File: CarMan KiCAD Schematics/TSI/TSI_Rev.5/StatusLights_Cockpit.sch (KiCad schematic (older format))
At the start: 21 parts, among them U1 RDE03110S12

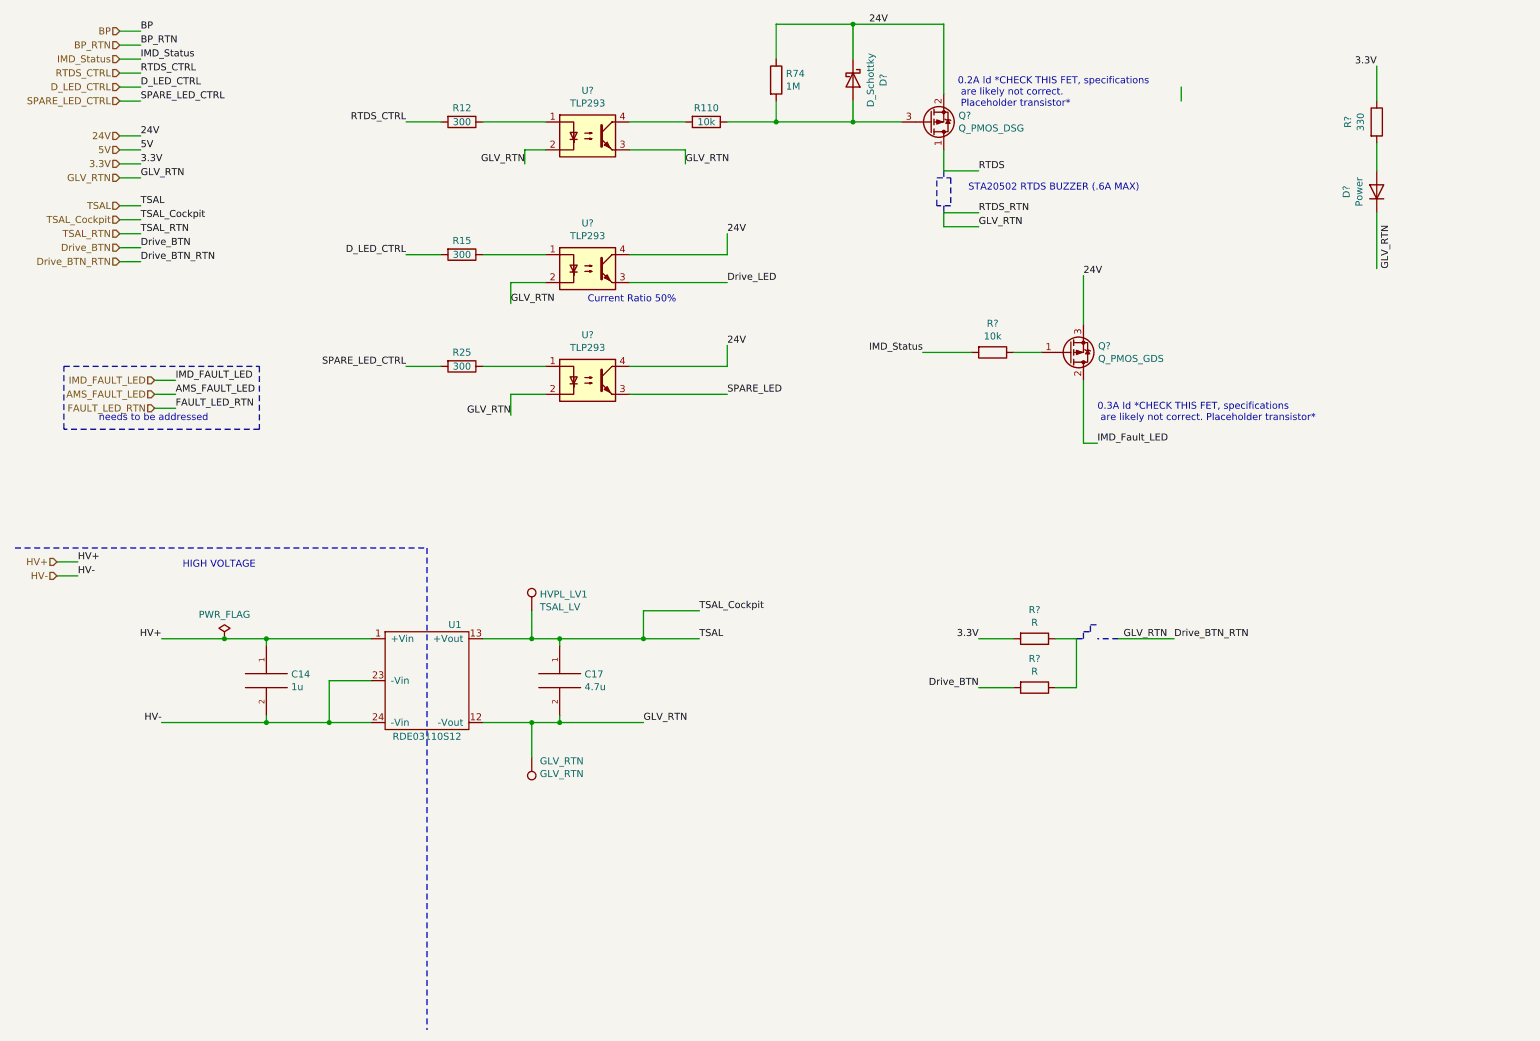
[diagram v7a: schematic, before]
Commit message: Res/Cap Value Updates & Organizational
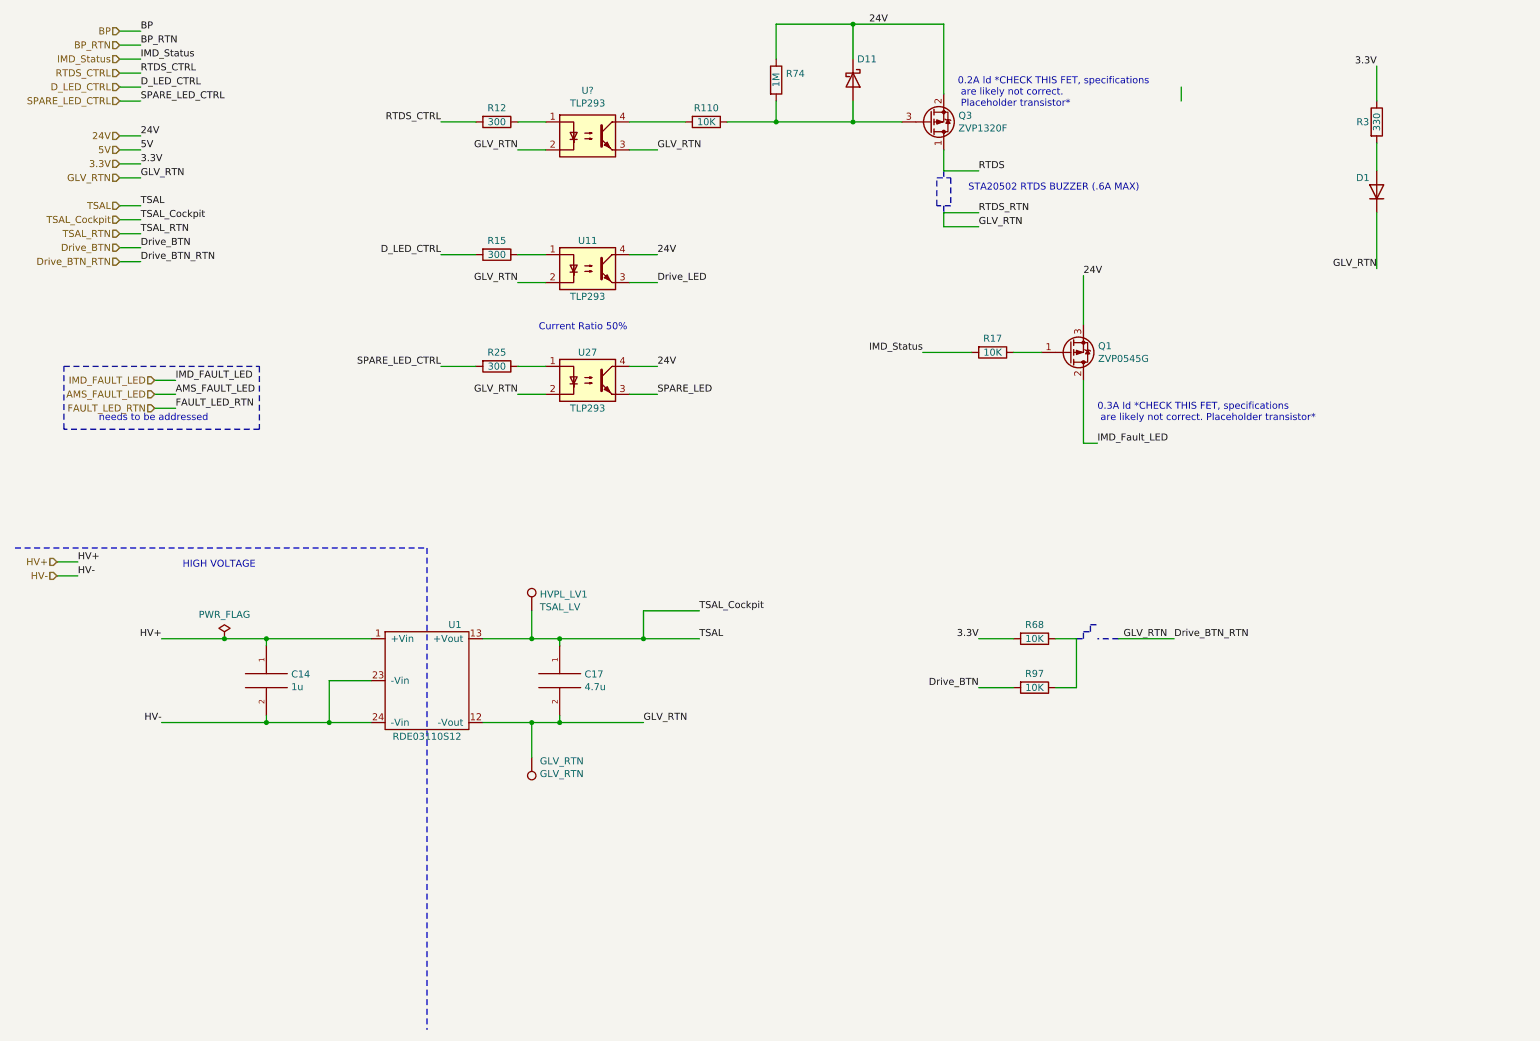
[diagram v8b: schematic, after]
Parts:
- Q1: renamed from Q?; value Q_PMOS_GDS -> ZVP0545G
- Q3: renamed from Q?; value Q_PMOS_DSG -> ZVP1320F
- R110: value 10k -> 10K
- R17: renamed from R?; value 10k -> 10K
- R68, R97: renamed from R?; value R -> 10K
- gave numbers to parts that had none: 5
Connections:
- wire segments 94 -> 88
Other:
- moved on the sheet: R12, R15, R25
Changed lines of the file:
@@
 EESchema Schematic File Version 4
-LIBS:TSI_Rev.5-cache
-EELAYER 29 0
+EELAYER 30 0
 EELAYER END
 $Descr A4 11693 8268
@@
 $EndDescr
 $Comp
-L Device:R R?
+L Device:R R3
 U 1 1 5F9997DD
 P 10200 1300
-F 0 "R?" V 9993 1300 50  0000 C CNN
-F 1 "330" V 10084 1300 50  0000 C CNN
+F 0 "R3" H 10100 1300 50  0000 C CNN
+F 1 "330" V 10200 1300 50  0000 C CNN
 F 2 "" V 10130 1300 50  0001 C CNN
 F 3 "~" H 10200 1300 50  0001 C CNN
@@
 $EndComp
 $Comp
-L Device:D D?
+L Device:D D1
 U 1 1 5F99A6B1
 P 10200 1800
-F 0 "D?" H 10200 2017 50  0000 C CNN
-F 1 "Power" H 10200 1926 50  0000 C CNN
+F 0 "D1" V 10300 1900 50  0000 C CNN
+F 1 "Power" H 10200 1926 50  0001 C CNN
 F 2 "" H 10200 1800 50  0001 C CNN
 F 3 "~" H 10200 1800 50  0001 C CNN
@@
 3.3V
 $Comp
-L TSI_Rev.5-rescue:TLP293-CarMan_KiCAD_Library-TSI_Rev.5-rescue U?
+L TSI_Rev.5-rescue:TLP293-CarMan_KiCAD_Library-TSI_Rev.5-rescue U11
 U 1 1 5F9A966C
 P 4550 2350
-F 0 "U?" H 4550 2675 50  0000 C CNN
-F 1 "TLP293" H 4550 2584 50  0000 C CNN
+F 0 "U11" H 4550 2550 50  0000 C CNN
+F 1 "TLP293" H 4550 2150 50  0000 C CNN
 F 2 "Package_SO:SOIC-4_4.55x2.6mm_P1.27mm" H 4350 2150 50  0001 L CIN
 F 3 "" H 4550 2350 50  0001 L CNN
@@
 $EndComp
 $Comp
-L TSI_Rev.5-rescue:TLP293-CarMan_KiCAD_Library-TSI_Rev.5-rescue U?
+L TSI_Rev.5-rescue:TLP293-CarMan_KiCAD_Library-TSI_Rev.5-rescue U27
 U 1 1 5F9AA400
 P 4550 3150
-F 0 "U?" H 4550 3475 50  0000 C CNN
-F 1 "TLP293" H 4550 3384 50  0000 C CNN
+F 0 "U27" H 4550 3350 50  0000 C CNN
+F 1 "TLP293" H 4550 2950 50  0000 C CNN
 F 2 "Package_SO:SOIC-4_4.55x2.6mm_P1.27mm" H 4350 2950 50  0001 L CIN
 F 3 "" H 4550 3150 50  0001 L CNN
@@
 	1    0    0    -1
 $EndComp
-Wire Wire Line
-	4850 2250 5550 2250
-Wire Wire Line
-	5550 2250 5550 2100
-Wire Wire Line
-	4850 2450 5550 2450
-Wire Wire Line
-	4850 3050 5550 3050
-Wire Wire Line
-	5550 3050 5550 2900
-Wire Wire Line
-	4850 3250 5550 3250
-Wire Wire Line
-	4250 2450 4000 2450
-Wire Wire Line
-	4000 2450 4000 2600
-Wire Wire Line
-	4250 3250 4000 3250
-Wire Wire Line
-	4000 3250 4000 3400
-$Comp
-L CarMan_KiCAD_Library:D_Schottky D?
+$Comp
+L CarMan_KiCAD_Library:D_Schottky D11
 U 1 1 5F9B6857
 P 6450 1000
-F 0 "D?" H 6450 1217 50  0000 C CNN
-F 1 "D_Schottky" H 6450 1126 50  0000 C CNN
+F 0 "D11" V 6300 1100 50  0000 C CNN
+F 1 "D_Schottky" H 6450 1126 50  0001 C CNN
 F 2 "" H 6450 1000 50  0001 C CNN
 F 3 "~" H 6450 1000 50  0001 C CNN
@@
 	0    1    1    0
 $EndComp
-Wire Wire Line
-	4100 1500 4100 1600
 $Comp
 L Device:R R12
 U 1 1 5F9BA8EE
-P 3650 1300
-F 0 "R12" V 3550 1300 50  0000 C CNN
-F 1 "300" V 3650 1300 50  0000 C CNN
-F 2 "" V 3580 1300 50  0001 C CNN
-F 3 "~" H 3650 1300 50  0001 C CNN
-	1    3650 1300
-	0    1    1    0
-$EndComp
-Wire Wire Line
-	3500 1300 3250 1300
-Text Label 3250 1300 2    50   ~ 0
+P 3900 1300
+F 0 "R12" V 3800 1300 50  0000 C CNN
+F 1 "300" V 3900 1300 50  0000 C CNN
+F 2 "" V 3830 1300 50  0001 C CNN
+F 3 "~" H 3900 1300 50  0001 C CNN
+	1    3900 1300
+	0    1    1    0
+$EndComp
+Wire Wire Line
+	3750 1300 3500 1300
+Text Label 3500 1300 2    50   ~ 0
 RTDS_CTRL
-Text Label 4100 1600 2    50   ~ 0
+Text Label 4050 1500 2    50   ~ 0
 GLV_RTN
 $Comp
@@
 P 5400 1300
 F 0 "R110" V 5300 1300 50  0000 C CNN
-F 1 "10k" V 5400 1300 50  0000 C CNN
+F 1 "10K" V 5400 1300 50  0000 C CNN
 F 2 "" V 5330 1300 50  0001 C CNN
 F 3 "~" H 5400 1300 50  0001 C CNN
@@
 P 5900 1000
 F 0 "R74" H 5970 1046 50  0000 L CNN
-F 1 "1M" H 5970 955 50  0000 L CNN
+F 1 "1M" V 5900 950 50  0000 L CNN
 F 2 "" V 5830 1000 50  0001 C CNN
 F 3 "~" H 5900 1000 50  0001 C CNN
@@
 L Device:R R15
 U 1 1 5F9DEF51
-P 3650 2250
-F 0 "R15" V 3550 2250 50  0000 C CNN
-F 1 "300" V 3650 2250 50  0000 C CNN
-F 2 "" V 3580 2250 50  0001 C CNN
-F 3 "~" H 3650 2250 50  0001 C CNN
-	1    3650 2250
-	0    1    1    0
-$EndComp
-Wire Wire Line
-	3800 2250 4250 2250
-Wire Wire Line
-	3500 2250 3250 2250
-Text Label 5550 2100 0    50   ~ 0
+P 3900 2250
+F 0 "R15" V 3800 2250 50  0000 C CNN
+F 1 "300" V 3900 2250 50  0000 C CNN
+F 2 "" V 3830 2250 50  0001 C CNN
+F 3 "~" H 3900 2250 50  0001 C CNN
+	1    3900 2250
+	0    1    1    0
+$EndComp
+Wire Wire Line
+	3750 2250 3500 2250
+Text Label 5050 2250 0    50   ~ 0
 24V
-Text Label 5550 2450 0    50   ~ 0
+Text Label 5050 2450 0    50   ~ 0
 Drive_LED
-Text Label 4000 2600 0    50   ~ 0
-GLV_RTN
-Text Label 3250 2250 2    50   ~ 0
+Text Label 4050 2450 2    50   ~ 0
+GLV_RTN
+Text Label 3500 2250 2    50   ~ 0
 D_LED_CTRL
 Wire Wire Line
@@
 Wire Wire Line
 	6450 600  7100 600
-Wire Wire Line
-	5250 1500 5250 1600
-Wire Wire Line
-	4250 1500 4100 1500
-Wire Wire Line
-	4250 1300 3800 1300
 $Comp
 L TSI_Rev.5-rescue:TLP293-CarMan_KiCAD_Library-TSI_Rev.5-rescue U?
@@
 	1    0    0    -1
 $EndComp
-Wire Wire Line
-	4850 1500 5250 1500
-Text Label 5250 1600 0    50   ~ 0
+Text Label 5050 1500 0    50   ~ 0
 GLV_RTN
 $Comp
 L Device:R R25
 U 1 1 5F9F8E38
-P 3650 3050
-F 0 "R25" V 3550 3050 50  0000 C CNN
-F 1 "300" V 3650 3050 50  0000 C CNN
-F 2 "" V 3580 3050 50  0001 C CNN
-F 3 "~" H 3650 3050 50  0001 C CNN
-	1    3650 3050
-	0    1    1    0
-$EndComp
-Wire Wire Line
-	3800 3050 4250 3050
-Wire Wire Line
-	3500 3050 3250 3050
-Text Label 4000 3400 2    50   ~ 0
-GLV_RTN
-Text Label 5550 3250 0    50   ~ 0
+P 3900 3050
+F 0 "R25" V 3800 3050 50  0000 C CNN
+F 1 "300" V 3900 3050 50  0000 C CNN
+F 2 "" V 3830 3050 50  0001 C CNN
+F 3 "~" H 3900 3050 50  0001 C CNN
+	1    3900 3050
+	0    1    1    0
+$EndComp
+Wire Wire Line
+	3750 3050 3500 3050
+Text Label 4050 3250 2    50   ~ 0
+GLV_RTN
+Text Label 5050 3250 0    50   ~ 0
 SPARE_LED
-Text Label 5550 2900 0    50   ~ 0
+Text Label 5050 3050 0    50   ~ 0
 24V
-Text Label 3250 3050 2    50   ~ 0
+Text Label 3500 3050 2    50   ~ 0
 SPARE_LED_CTRL
 $Comp
-L Device:Q_PMOS_DSG Q?
+L Device:Q_PMOS_DSG Q3
 U 1 1 5FA04A44
 P 7000 1300
-F 0 "Q?" H 7205 1254 50  0000 L CNN
-F 1 "Q_PMOS_DSG" H 7205 1345 50  0000 L CNN
+F 0 "Q3" H 7205 1254 50  0000 L CNN
+F 1 "ZVP1320F" H 7205 1345 50  0000 L CNN
 F 2 "" H 7200 1400 50  0001 C CNN
 F 3 "~" H 7000 1300 50  0001 C CNN
@@
 TSAL_Cockpit
 $Comp
-L Device:R R?
+L Device:R R17
 U 1 1 5FA5E58C
 P 7450 2950
-F 0 "R?" V 7243 2950 50  0000 C CNN
-F 1 "10k" V 7334 2950 50  0000 C CNN
+F 0 "R17" V 7350 2950 50  0000 C CNN
+F 1 "10K" V 7450 2950 50  0000 C CNN
 F 2 "" V 7380 2950 50  0001 C CNN
 F 3 "~" H 7450 2950 50  0001 C CNN
@@
 IMD_Status
 $Comp
-L Device:Q_PMOS_GDS Q?
+L Device:Q_PMOS_GDS Q1
 U 1 1 5FA66ED5
 P 8000 2950
-F 0 "Q?" H 8205 2904 50  0000 L CNN
-F 1 "Q_PMOS_GDS" H 8205 2995 50  0000 L CNN
+F 0 "Q1" H 8205 2904 50  0000 L CNN
+F 1 "ZVP0545G" H 8205 2995 50  0000 L CNN
 F 2 "" H 8200 3050 50  0001 C CNN
 F 3 "~" H 8000 2950 50  0001 C CNN
@@
 Text Notes 7200 1200 0    50   ~ 0
 0.2A Id *CHECK THIS FET, specifications\n are likely not correct.\n Placeholder transistor*
-Text Notes 4550 2600 0    50   ~ 0
+Text Notes 4200 2800 0    50   ~ 0
 Current Ratio 50%
 $Comp
@@
 HIGH VOLTAGE\n
 $Comp
-L Device:R R?
+L Device:R R68
 U 1 1 5FA84662
 P 7750 5000
-F 0 "R?" V 7543 5000 50  0000 C CNN
-F 1 "R" V 7634 5000 50  0000 C CNN
+F 0 "R68" V 7650 5000 50  0000 C CNN
+F 1 "10K" V 7750 5000 50  0000 C CNN
 F 2 "" V 7680 5000 50  0001 C CNN
 F 3 "~" H 7750 5000 50  0001 C CNN
@@
 $EndComp
 $Comp
-L Device:R R?
+L Device:R R97
 U 1 1 5FA84F23
 P 7750 5350
-F 0 "R?" V 7543 5350 50  0000 C CNN
-F 1 "R" V 7634 5350 50  0000 C CNN
+F 0 "R97" V 7650 5350 50  0000 C CNN
+F 1 "10K" V 7750 5350 50  0000 C CNN
 F 2 "" V 7680 5350 50  0001 C CNN
 F 3 "~" H 7750 5350 50  0001 C CNN
@@
 Text Label 1350 2000 0    50   ~ 0
 TSAL_Cockpit
-Text Label 10300 2350 1    50   ~ 0
+Text Label 10200 2350 2    50   ~ 0
 GLV_RTN
 Wire Wire Line
@@
 Text Label 1350 2200 0    50   ~ 0
 Drive_BTN
+Wire Wire Line
+	5050 3250 4850 3250
+Wire Wire Line
+	5050 3050 4850 3050
+Wire Wire Line
+	4250 3050 4050 3050
+Wire Wire Line
+	4250 3250 4050 3250
+Wire Wire Line
+	5050 2250 4850 2250
+Wire Wire Line
+	5050 2450 4850 2450
+Wire Wire Line
+	4250 2450 4050 2450
+Wire Wire Line
+	4250 2250 4050 2250
+Wire Wire Line
+	4250 1300 4050 1300
+Wire Wire Line
+	4250 1500 4050 1500
+Wire Wire Line
+	5050 1500 4850 1500
 $EndSCHEMATC
